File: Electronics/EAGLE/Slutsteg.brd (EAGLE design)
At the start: 100 x 160 mm, 177 parts, among them CN1 OSTYK33102030-2, CN2 OSTYK33102030-2, CN3 OSTYK33102030-2, IC1 SPX1117M3-L-3-3_TR, IC10 LM324D, IC11 L78M12ABDT-TR, IC2 L78M12ABDT-TR, IC3 ESP32-WROVER-IE-4MB, IC4 TM8211, IC5 LM324D, IC6 TPA3244DDWR, IC7 TPA3251D2DDVR, IC8 LM324D, IC9 LM324D, J1 0532610671, J2 JW-PJ-307-4H, J4 B4P-VH_LF__SN_, SW3 PDB181-K420F-103A2

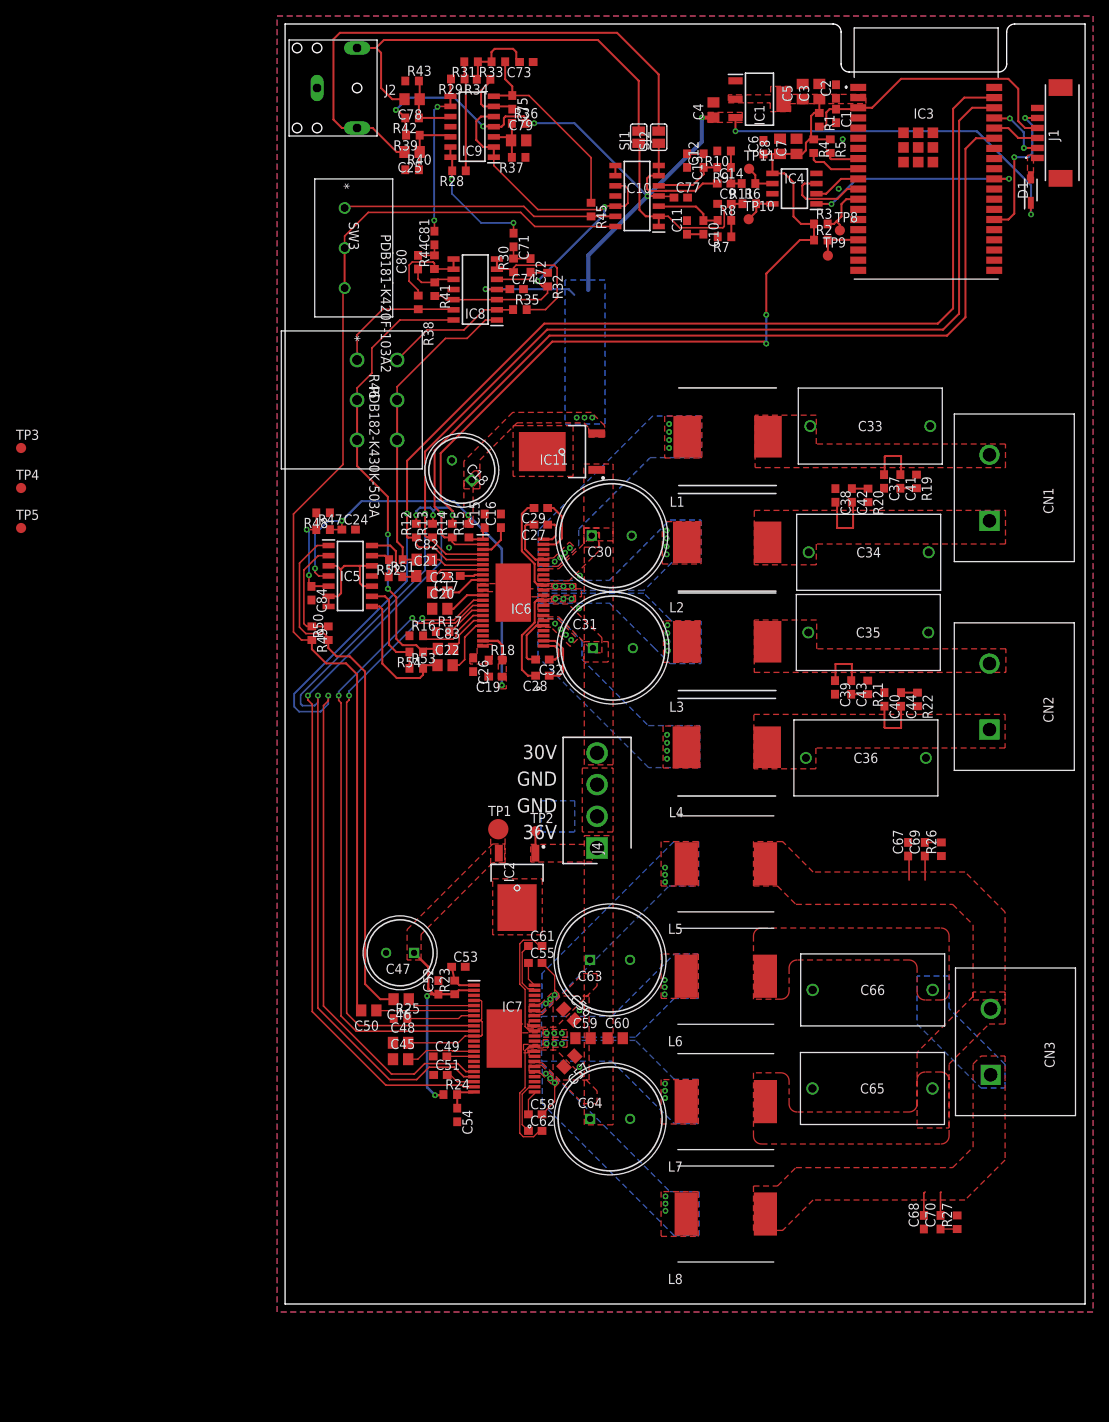
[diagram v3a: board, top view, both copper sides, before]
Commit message: TPs och Viastiching
TP,VIAstich,borrhål
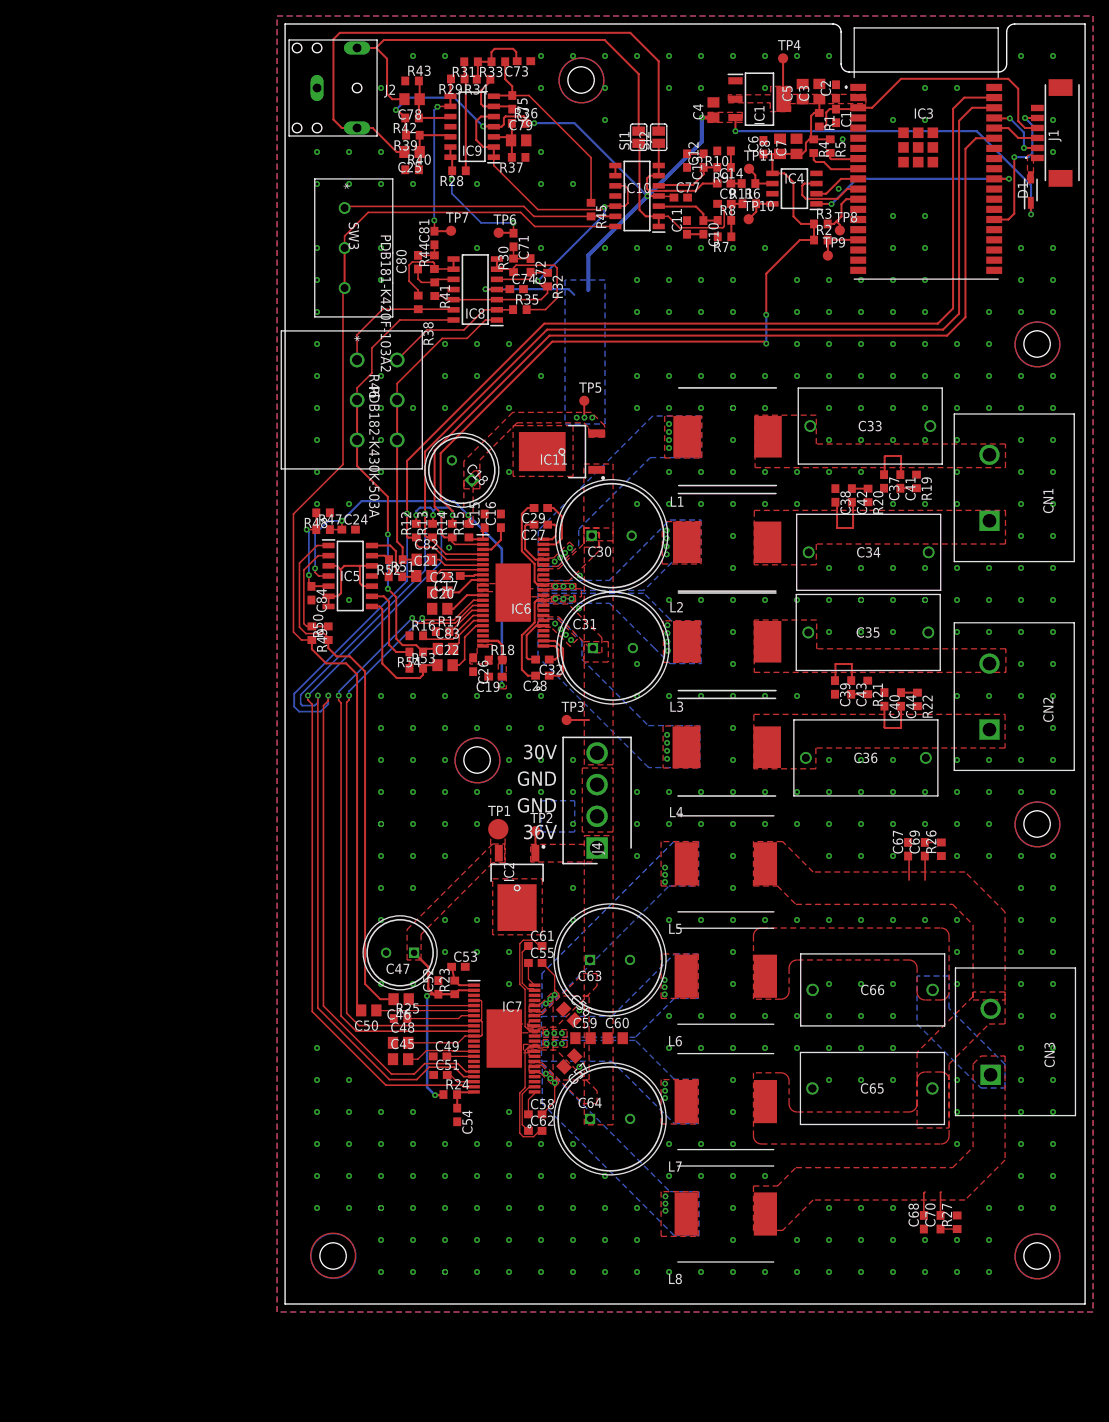
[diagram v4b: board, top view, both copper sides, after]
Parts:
- added TP6, TP7: TPB1,27, testpad:B1,27
- moved TP4 109.3 mm to (62.2, 155.7)
- moved TP3 76.2 mm to (35.2, 73.0)
- moved TP5 72.2 mm to (37.4, 112.9)
- moved C73 0.32 mm to (29.9, 155.3)
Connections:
- net LEFT: now also TP6.TP
- net RIGHT: now also TP7.TP
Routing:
- net +3V3: track 112.2 -> 117.3 mm
- net PVDD: track 0.00 -> 2.80 mm
- net VDD: track 195.7 -> 197.8 mm
- net RIGHT: track 20.8 -> 22.9 mm
- net LEFT: track 16.4 -> 18.3 mm
- net SIG_IN_LEFT: track 70.8 -> 71.8 mm
- added copper zone on layer 1, net ISOLATION
- added copper zone on layer 16, net ISOLATION
- added copper zone on layer 1, net ISOLATION1
- added copper zone on layer 1, net ISOLATION2
- added copper zone on layer 1, net ISOLATION3
- added copper zone on layer 1, net ISOLATION4
- added copper zone on layer 16, net ISOLATION5
- added copper zone on layer 16, net ISOLATION6
- added copper zone on layer 16, net ISOLATION7
- added copper zone on layer 16, net ISOLATION8
- added copper zone on layer 16, net ISOLATION9

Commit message: Moved labels in layout.
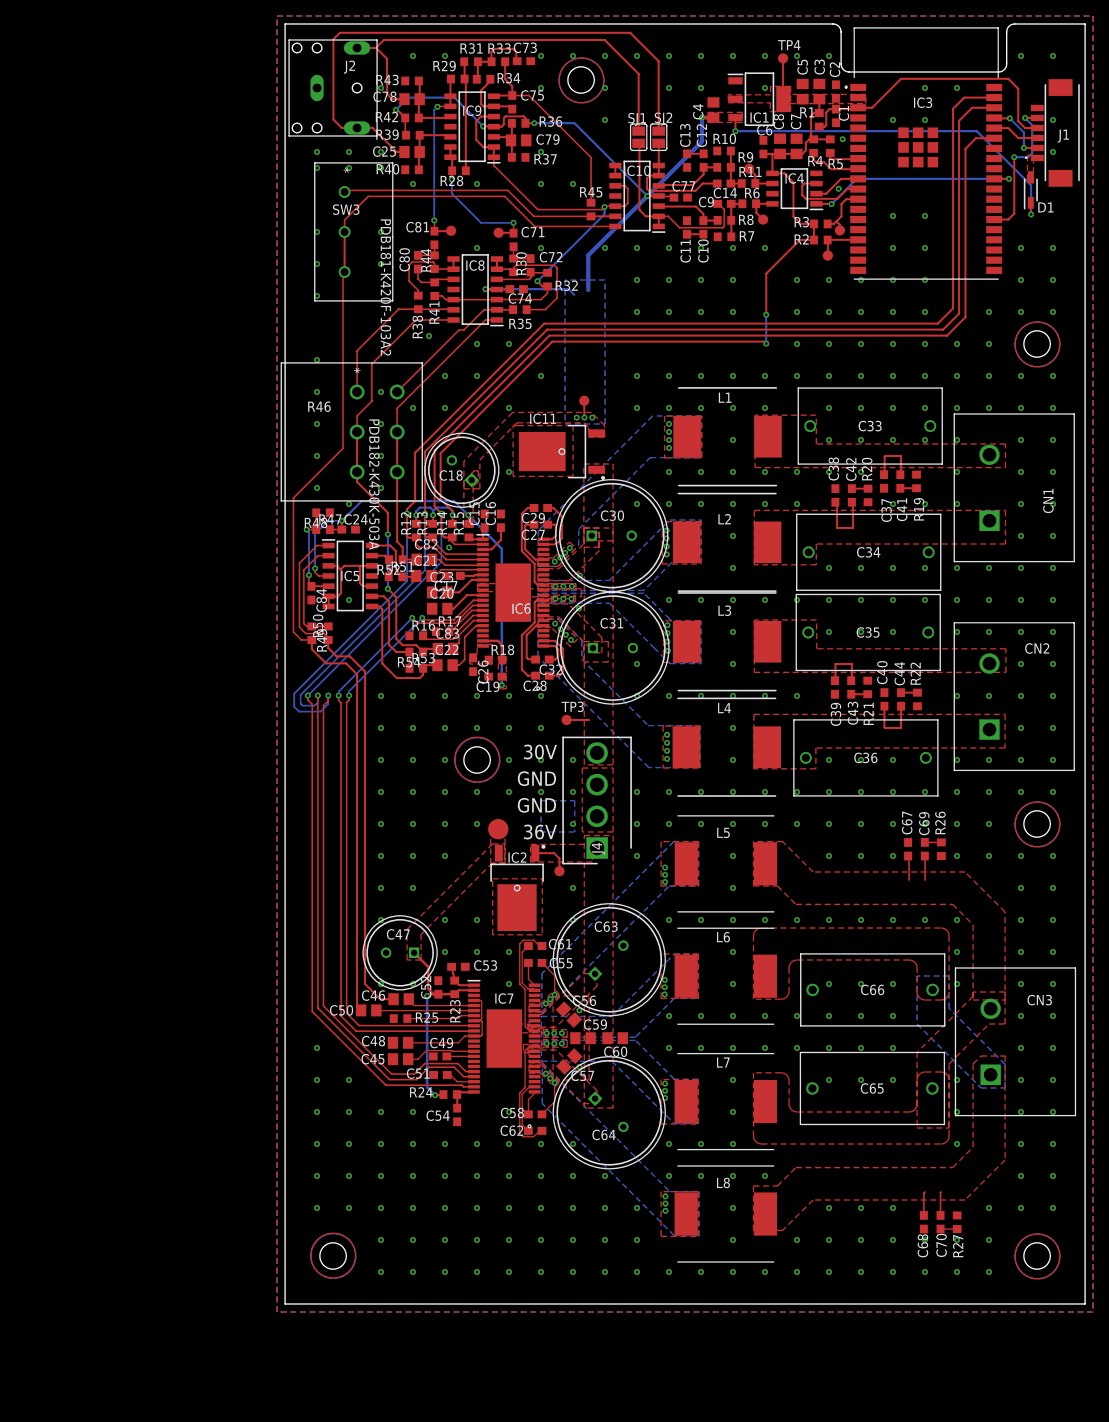
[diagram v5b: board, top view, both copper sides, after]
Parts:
- added U$3, U$4: V5618A, V5618A:V5618A
- moved TP2 5.83 mm to (34.3, 54.1)
- moved R46 4.00 mm to (9.00, 114.0)
- moved C64 2.61 mm to (38.8, 25.7), turned to 315 degrees
- moved SW3 2.00 mm to (7.44, 139.0)
- moved C63 1.86 mm to (38.8, 41.3), turned to 45 degrees
- moved TP10 1.80 mm to (59.8, 135.6)
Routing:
- net N$74: track 16.6 -> 19.4 mm
- net INPUT_B_SLAVE: track 141.0 -> 143.8 mm
- net PVDD2: track 2.76 -> 4.88 mm
- net INPUT_D: track 39.8 -> 38.0 mm
- net N$71: track 17.1 -> 18.8 mm
- net INPUT_B: track 56.9 -> 55.7 mm
- net N$4: track 34.4 -> 35.3 mm
- added copper zone on layer 16, net ISOLATION1
- added copper zone on layer 1, net ISOLATION7
- removed copper zone on layer 1, net ISOLATION1
- removed copper zone on layer 16, net ISOLATION7

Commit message: Finished the first draft and exported the Gerber files.
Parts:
- moved C35 0.10 mm to (80.5, 83.9)
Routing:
- net +3V3: vias 5 -> 10
- added copper zone on layer 16, net +3V3
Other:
- outline, holes or cut-outs redrawn
- board text added: "TSTE93: Ruski Hardbass 10/03-2021 V:1.0 By: JS, JO & VE."
